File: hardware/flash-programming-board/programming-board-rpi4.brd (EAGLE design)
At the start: 80 x 80 mm, 3 parts, among them J1 RPI-CONNECTOR, U1 SST39SF010A-70-4C-NHEMICROCHI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

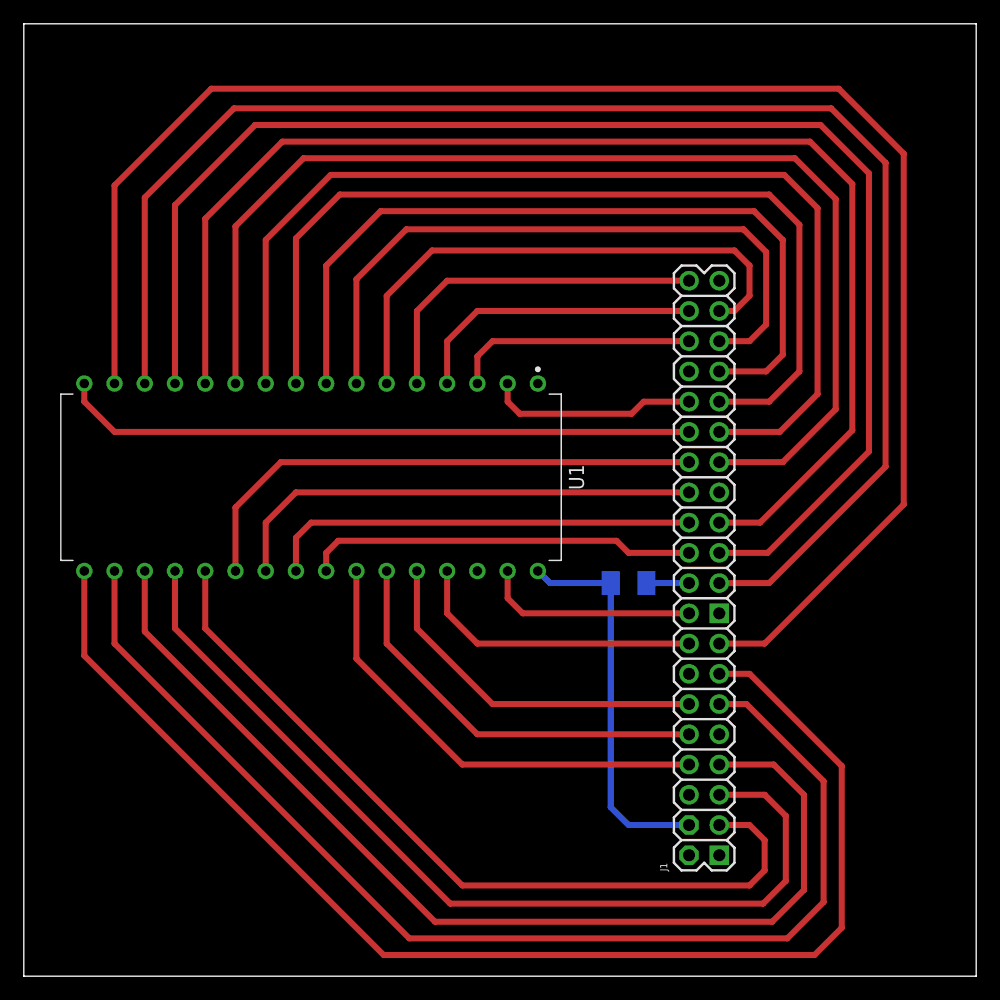
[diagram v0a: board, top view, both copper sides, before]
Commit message: increased size of traces
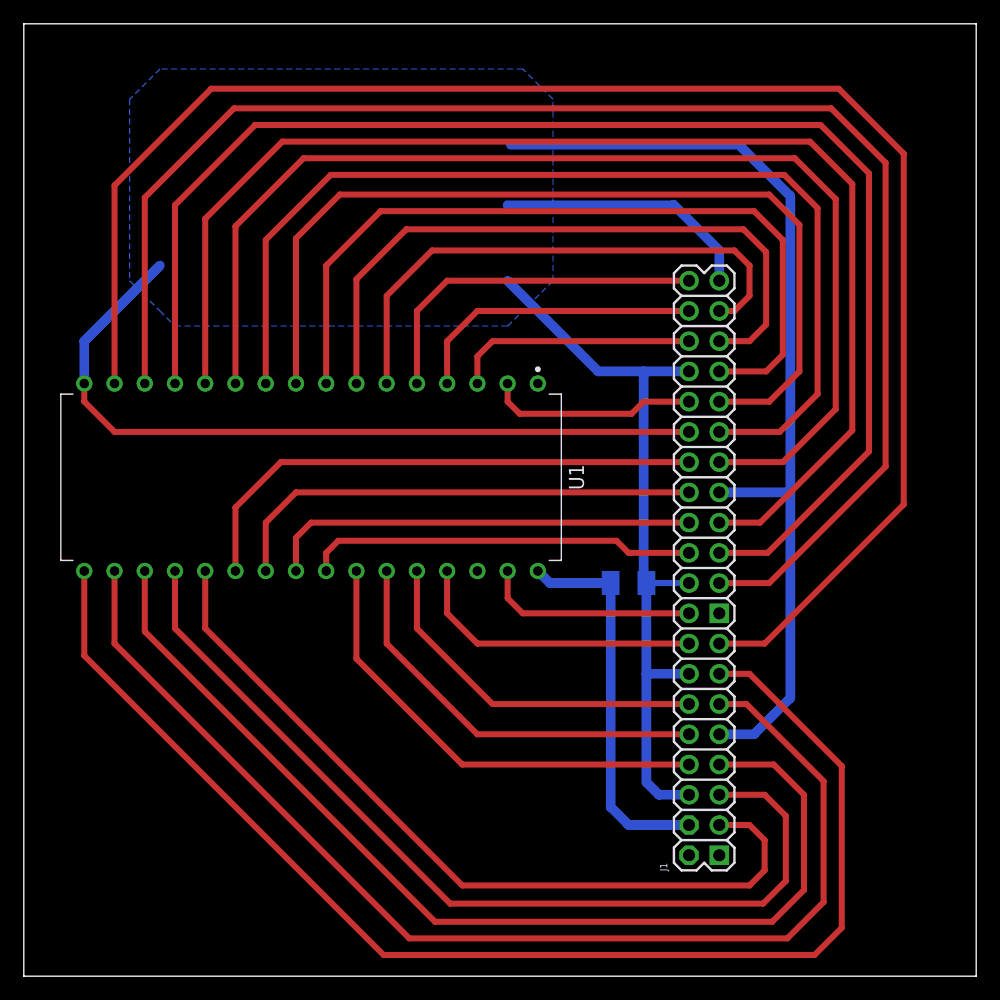
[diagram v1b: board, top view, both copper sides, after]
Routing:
- net GND: track 57.0 -> 232.6 mm
- added copper zone on layer 16, net GND
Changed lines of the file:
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@@
 <contactref element="U1" pad="32"/>
 <contactref element="C1" pad="1"/>
-<wire x1="55.88" y1="12.7" x2="50.8" y2="12.7" width="0.508" layer="16"/>
-<wire x1="49.3" y1="14.2" x2="49.3" y2="33.02" width="0.508" layer="16"/>
-<wire x1="50.8" y1="12.7" x2="49.3" y2="14.2" width="0.508" layer="16"/>
-<wire x1="49.3" y1="33.02" x2="44.196" y2="33.02" width="0.508" layer="16"/>
-<wire x1="44.196" y1="33.02" x2="43.18" y2="34.036" width="0.508" layer="16"/>
+<wire x1="55.88" y1="12.7" x2="50.8" y2="12.7" width="0.8128" layer="16"/>
+<wire x1="49.3" y1="14.2" x2="49.3" y2="33.02" width="0.8128" layer="16"/>
+<wire x1="50.8" y1="12.7" x2="49.3" y2="14.2" width="0.8128" layer="16"/>
+<wire x1="49.3" y1="33.02" x2="44.196" y2="33.02" width="0.8128" layer="16"/>
+<wire x1="44.196" y1="33.02" x2="43.18" y2="34.036" width="0.8128" layer="16"/>
 <wire x1="55.88" y1="12.7" x2="55.88" y2="10.16" width="0" layer="19" extent="1-1"/>
 </signal>
@@
 <wire x1="7.62" y1="45.72" x2="5.08" y2="48.26" width="0.508" layer="1"/>
 <wire x1="52.3" y1="33.02" x2="55.88" y2="33.02" width="0.508" layer="16"/>
-<wire x1="55.88" y1="50.8" x2="58.42" y2="58.42" width="0" layer="19" extent="1-1"/>
-<wire x1="55.88" y1="45.72" x2="55.88" y2="50.8" width="0" layer="19" extent="1-1"/>
-<wire x1="58.42" y1="40.64" x2="55.88" y2="45.72" width="0" layer="19" extent="1-1"/>
-<wire x1="55.88" y1="33.02" x2="58.42" y2="40.64" width="0" layer="19" extent="1-1"/>
-<wire x1="55.88" y1="25.4" x2="55.88" y2="33.02" width="0" layer="19" extent="1-1"/>
-<wire x1="58.42" y1="20.32" x2="55.88" y2="25.4" width="0" layer="19" extent="1-1"/>
-<wire x1="55.88" y1="15.24" x2="58.42" y2="20.32" width="0" layer="19" extent="1-1"/>
+<polygon width="0.508" layer="16">
+<vertex x="8.89" y="73.66"/>
+<vertex x="8.89" y="58.42"/>
+<vertex x="11.43" y="55.88"/>
+<vertex x="12.7" y="54.61"/>
+<vertex x="40.64" y="54.61"/>
+<vertex x="44.45" y="58.42"/>
+<vertex x="44.45" y="73.66"/>
+<vertex x="41.91" y="76.2"/>
+<vertex x="11.43" y="76.2"/>
+</polygon>
+<wire x1="5.08" y1="49.784" x2="5.08" y2="53.34" width="0.8128" layer="16"/>
+<wire x1="5.08" y1="53.34" x2="11.43" y2="59.69" width="0.8128" layer="16"/>
+<wire x1="48.26" y1="50.8" x2="40.64" y2="58.42" width="0.8128" layer="16"/>
+<wire x1="55.88" y1="50.8" x2="52.07" y2="50.8" width="0.8128" layer="16"/>
+<wire x1="52.07" y1="50.8" x2="48.26" y2="50.8" width="0.8128" layer="16"/>
+<wire x1="58.42" y1="58.42" x2="58.42" y2="60.96" width="0.8128" layer="16"/>
+<wire x1="58.42" y1="60.96" x2="54.61" y2="64.77" width="0.8128" layer="16"/>
+<wire x1="54.61" y1="64.77" x2="40.64" y2="64.77" width="0.8128" layer="16"/>
+<wire x1="52.3" y1="33.02" x2="52.07" y2="33.25" width="0.508" layer="16"/>
+<wire x1="52.07" y1="33.25" x2="52.07" y2="50.8" width="0.8128" layer="16"/>
+<wire x1="55.88" y1="15.24" x2="53.34" y2="15.24" width="0.8128" layer="16"/>
+<wire x1="53.34" y1="15.24" x2="52.3" y2="16.28" width="0.8128" layer="16"/>
+<wire x1="52.3" y1="16.28" x2="52.3" y2="25.4" width="0.8128" layer="16"/>
+<wire x1="52.3" y1="25.4" x2="52.3" y2="33.02" width="0.8128" layer="16"/>
+<wire x1="55.88" y1="25.4" x2="52.3" y2="25.4" width="0.8128" layer="16"/>
+<wire x1="58.42" y1="20.32" x2="61.341" y2="20.32" width="0.8128" layer="16"/>
+<wire x1="61.341" y1="20.32" x2="64.389" y2="23.368" width="0.8128" layer="16"/>
+<wire x1="64.389" y1="23.368" x2="64.389" y2="40.64" width="0.8128" layer="16"/>
+<wire x1="64.389" y1="40.64" x2="64.389" y2="65.532" width="0.8128" layer="16"/>
+<wire x1="60.071" y1="69.85" x2="40.894" y2="69.85" width="0.8128" layer="16"/>
+<wire x1="64.389" y1="65.532" x2="60.071" y2="69.85" width="0.8128" layer="16"/>
+<wire x1="58.42" y1="40.64" x2="64.389" y2="40.64" width="0.8128" layer="16"/>
 </signal>
 <signal name="WE">

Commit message: made the board slightly smaller so I can mill out of fr4
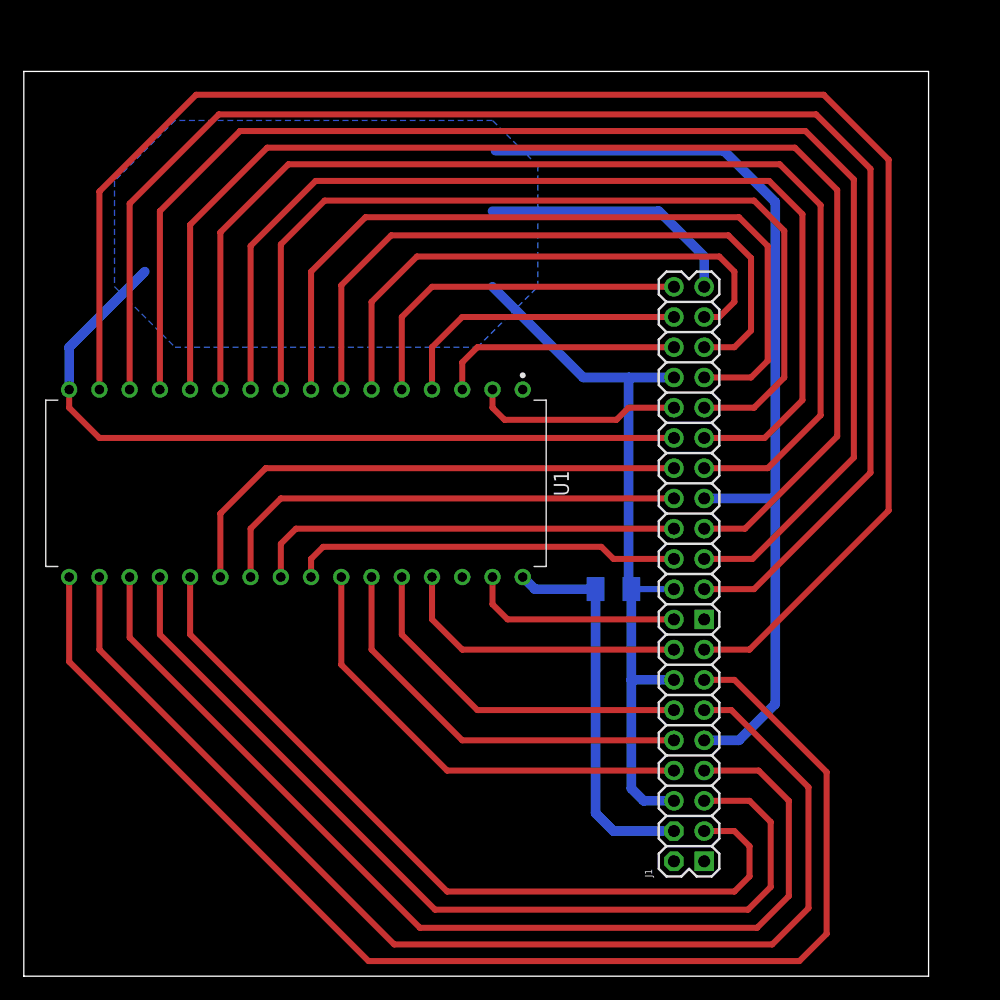
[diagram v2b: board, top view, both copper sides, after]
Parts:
- moved U1 1.37 mm to (22.9, 41.4)
- moved C1 1.37 mm to (49.5, 32.5)
- moved J1 1.37 mm to (55.9, 33.8)
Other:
- board size 80 x 80 mm -> 76 x 76 mm
